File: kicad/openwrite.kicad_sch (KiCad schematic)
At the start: 77 parts, among them J1 raspberry-pi-zero-with-test-p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, SW71 SW_SPST, U1 adafruit-kb2040, U2 adafruit-powerboost-1000c, U3 waveshare-2in-lcd-st7789v

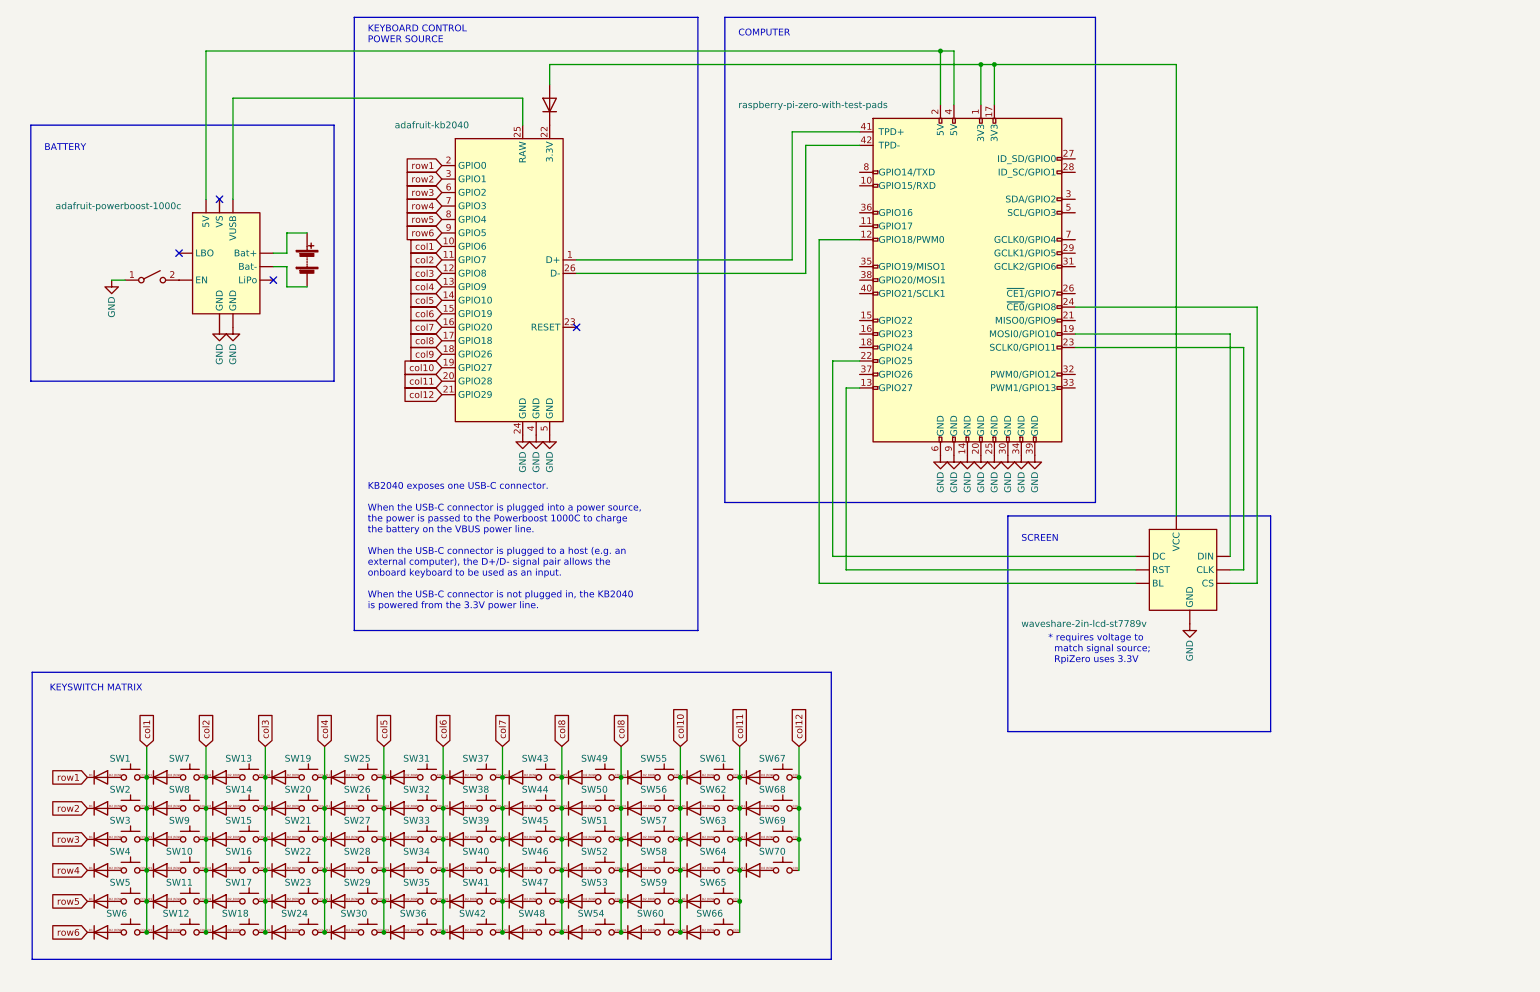
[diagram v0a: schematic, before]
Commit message: clean up schema, fix typos
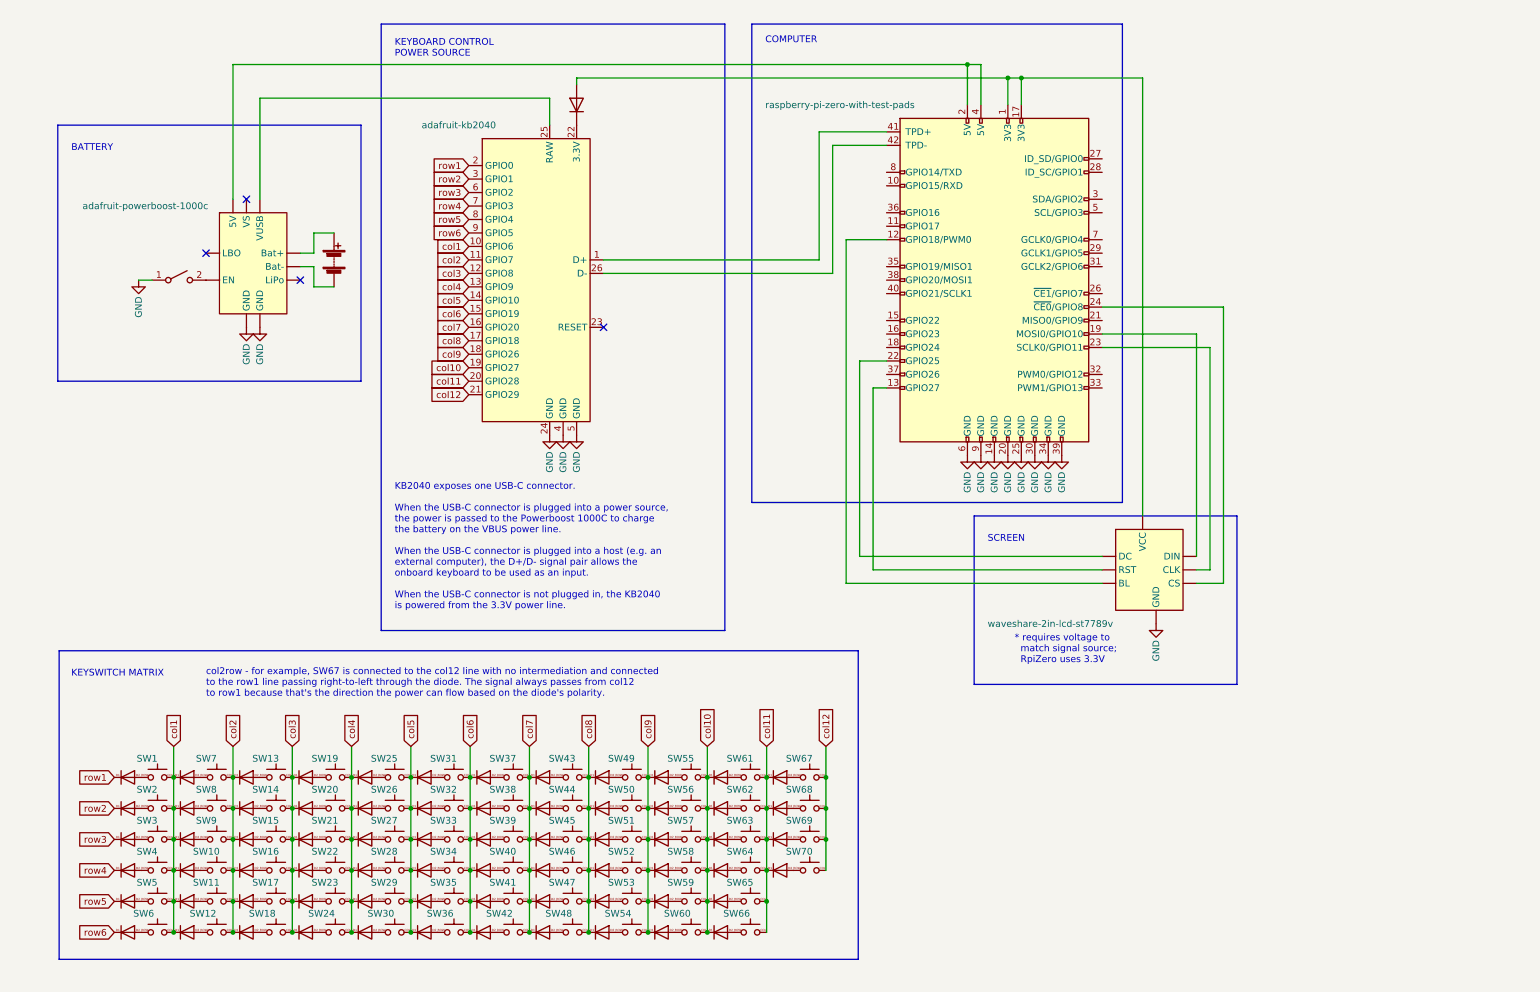
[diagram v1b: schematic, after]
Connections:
- net col8: no longer SW49.COL, SW50.COL, SW51.COL, SW52.COL, SW53.COL, SW54.COL, SW55.D1, SW56.D1, SW57.D1, SW58.D1, SW59.D1, SW60.D1
- net col9: now also SW49.COL, SW50.COL, SW51.COL, SW52.COL, SW53.COL, SW54.COL, SW55.D1, SW56.D1, SW57.D1, SW58.D1, SW59.D1, SW60.D1
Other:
- note added: "KB2040 exposes one USB-C connector. When the USB-C connector is plugged into a power source, the power is passed to the Powerboost 1000C to charge the battery on the VBUS power line. When the USB-C connector is plugged into a host (e.g. an external computer), the D+/D- signal pair allows the onboard keyboard to be used as an input. When the USB-C connector is not plugged in, the KB2040 is powered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"
- note added: "col2row - for example, SW67 is connected to the col12 line with no intermediation and connected to the row1 line passing right-to-left through the diode. The signal always passes from col12 to row1 because that's the direction the power can flow based on the diode's polarity."
- note removed: "KB2040 exposes one USB-C connector. When the USB-C connector is plugged into a power source, the power is passed to the Powerboost 1000C to charge the battery on the VBUS power line. When the USB-C connector is plugged to a host (e.g. an external computer), the D+/D- signal pair allows the onboard keyboard to be used as an input. When the USB-C connector is not plugged in, the KB2040 is powered f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"
- moved on the sheet: SW1, SW10, SW11, SW12, SW13, SW14, SW15, SW16, SW17, SW18, SW19, SW2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

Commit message: fix gateron-ks-33-diode symbol to remove extra pin
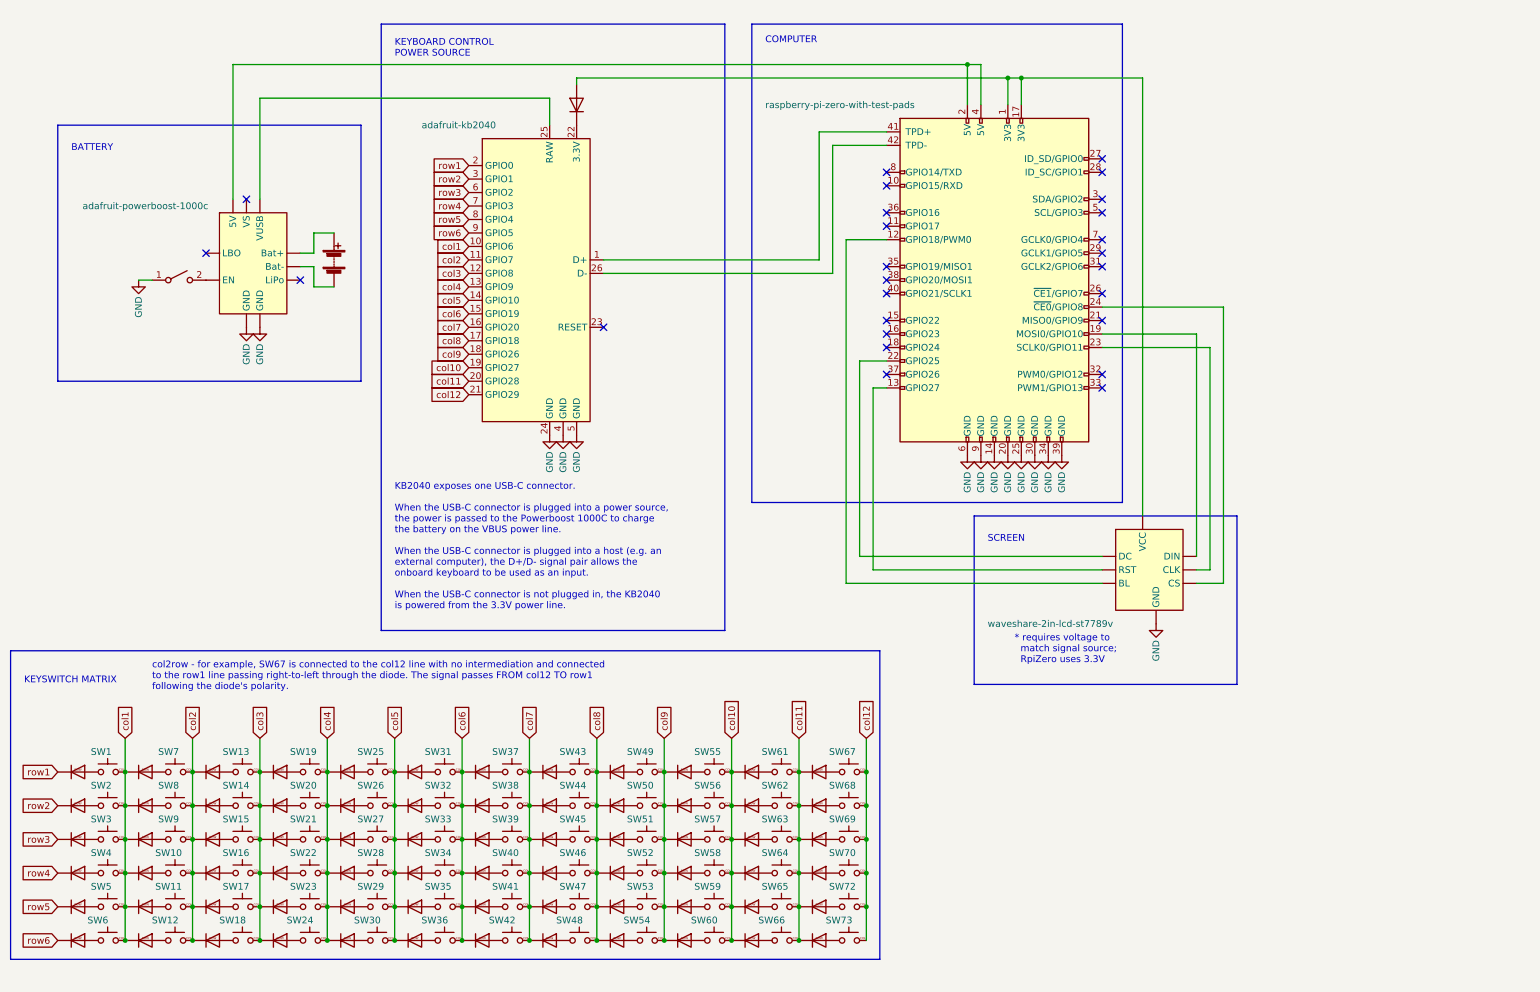
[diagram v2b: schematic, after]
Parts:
- added SW72, SW73: ~, openwrite:gateron-ks-33-diode, symbol openwrite:gateron-ks-33-diode
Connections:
- net col1: now also SW10.ROW, SW11.ROW, SW12.ROW, SW7.ROW, SW8.ROW, SW9.ROW; no longer SW10.D1, SW11.D1, SW12.D1, SW7.D1, SW8.D1, SW9.D1
- net col10: now also SW61.ROW, SW62.ROW, SW63.ROW, SW64.ROW, SW65.ROW, SW66.ROW; no longer SW61.D1, SW62.D1, SW63.D1, SW64.D1, SW65.D1, SW66.D1
- net col11: now also SW67.ROW, SW68.ROW, SW69.ROW, SW70.ROW, SW72.ROW, SW73.ROW; no longer SW67.D1, SW68.D1, SW69.D1, SW70.D1
- net col12: now also SW72.COL, SW73.COL
- net col2: now also SW13.ROW, SW14.ROW, SW15.ROW, SW16.ROW, SW17.ROW, SW18.ROW; no longer SW13.D1, SW14.D1, SW15.D1, SW16.D1, SW17.D1, SW18.D1
- net col3: now also SW19.ROW, SW20.ROW, SW21.ROW, SW22.ROW, SW23.ROW, SW24.ROW; no longer SW19.D1, SW20.D1, SW21.D1, SW22.D1, SW23.D1, SW24.D1
- net col4: now also SW25.ROW, SW26.ROW, SW27.ROW, SW28.ROW, SW29.ROW, SW30.ROW; no longer SW25.D1, SW26.D1, SW27.D1, SW28.D1, SW29.D1, SW30.D1
- net col5: now also SW31.ROW, SW32.ROW, SW33.ROW, SW34.ROW, SW35.ROW, SW36.ROW; no longer SW31.D1, SW32.D1, SW33.D1, SW34.D1, SW35.D1, SW36.D1
- net col6: now also SW37.ROW, SW38.ROW, SW39.ROW, SW40.ROW, SW41.ROW, SW42.ROW; no longer SW37.D1, SW38.D1, SW39.D1, SW40.D1, SW41.D1, SW42.D1
- net col7: now also SW43.ROW, SW44.ROW, SW45.ROW, SW46.ROW, SW47.ROW, SW48.ROW; no longer SW43.D1, SW44.D1, SW45.D1, SW46.D1, SW47.D1, SW48.D1
- net col8: now also SW49.ROW, SW50.ROW, SW51.ROW, SW52.ROW, SW53.ROW, SW54.ROW; no longer SW49.D1, SW50.D1, SW51.D1, SW52.D1, SW53.D1, SW54.D1
- net col9: now also SW55.ROW, SW56.ROW, SW57.ROW, SW58.ROW, SW59.ROW, SW60.ROW; no longer SW55.D1, SW56.D1, SW57.D1, SW58.D1, SW59.D1, SW60.D1
- net row1: now also SW1.ROW; no longer SW1.D1
- net row2: now also SW2.ROW; no longer SW2.D1
- net row3: now also SW3.ROW; no longer SW3.D1
- net row4: now also SW4.ROW; no longer SW4.D1
- net row5: now also SW5.ROW; no longer SW5.D1
- net row6: now also SW6.ROW; no longer SW6.D1
- no-connect marks 4 -> 26
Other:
- note added: "col2row - for example, SW67 is connected to the col12 line with no intermediation and connected to the row1 line passing right-to-left through the diode. The signal passes FROM col12 TO row1 following the diode's polarity."
- note removed: "col2row - for example, SW67 is connected to the col12 line with no intermediation and connected to the row1 line passing right-to-left through the diode. The signal always passes from col12 to row1 because that's the direction the power can flow based on the diode's polarity."

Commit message: Differentiate diode and keyswitch
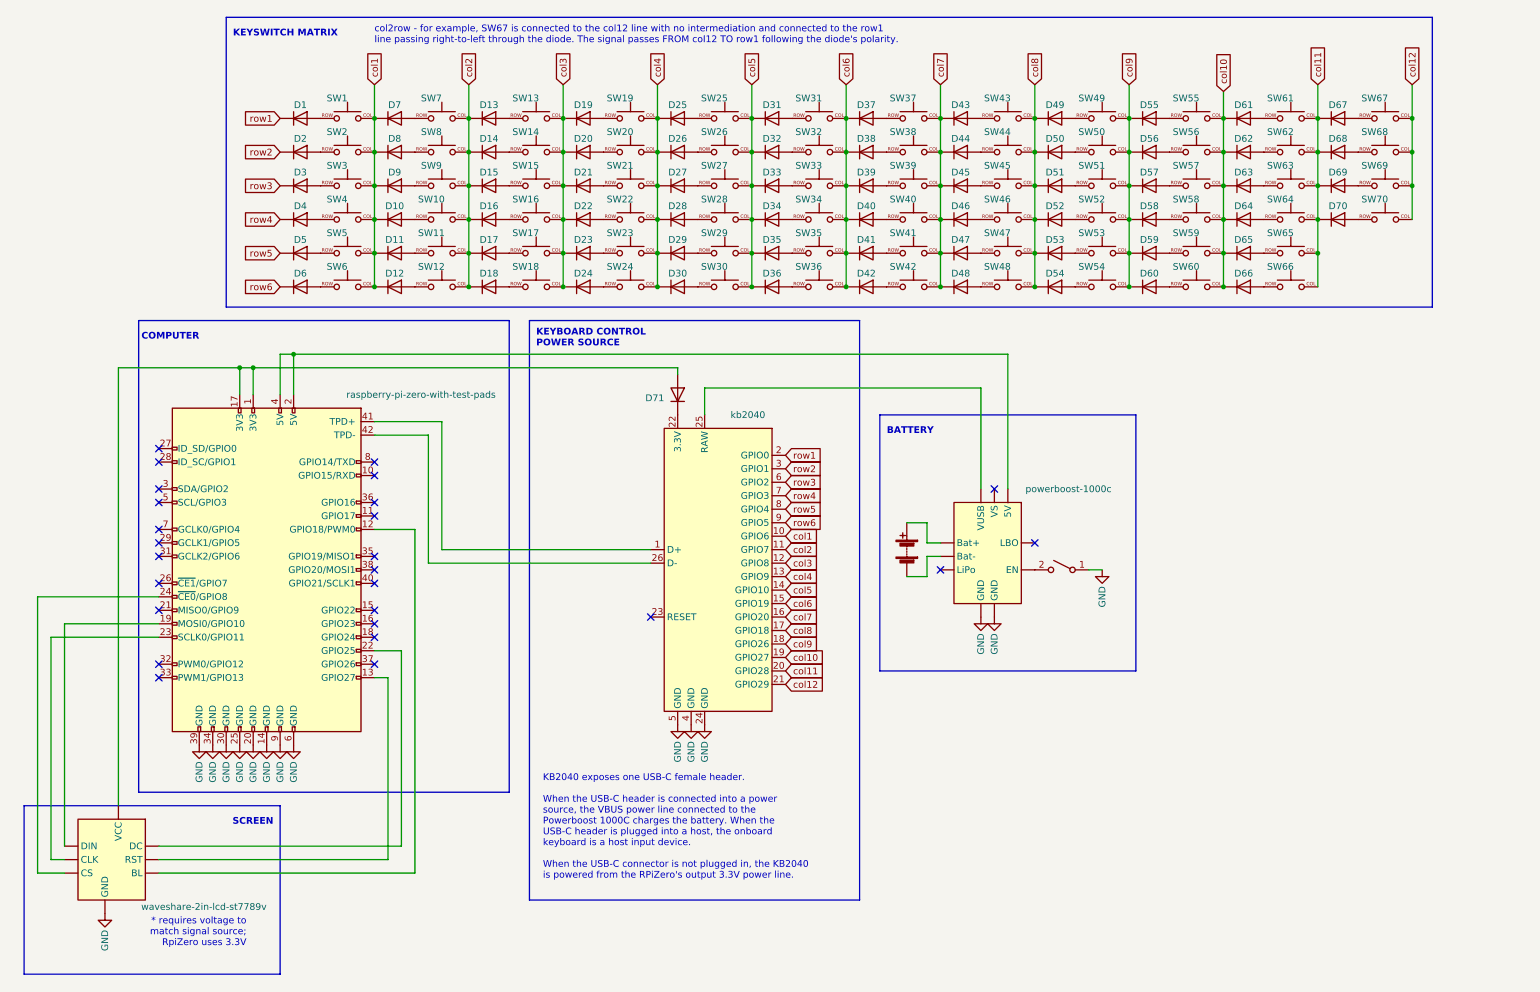
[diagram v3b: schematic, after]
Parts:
- removed D1: 1N4148, Diode_THT:D_DO-35_SOD27_P7.62mm_Horizontal, symbol Diode:1N4148
- removed SW10, SW11, SW12, SW13, SW14, SW15, SW16, SW17, SW18, SW19, SW2, SW20, SW21, SW22, SW23, SW24, SW25, SW26, SW27, SW28, SW29, SW3, SW30, SW31, SW32, SW33, SW34, SW35, SW36, SW37, SW38, SW39, SW4, SW40, SW41, SW42, SW43, SW44, SW45, SW46, SW47, SW48, SW49, SW5, SW50, SW51, SW52, SW53, SW54, SW55, SW56, SW57, SW58, SW59, SW6, SW60, SW61, SW62, SW63, SW64, SW65, SW66, SW67, SW68, SW69, SW7, SW70, SW72, SW73, SW8, SW9: ~, openwrite:gateron-ks-33-diode, symbol openwrite:gateron-ks-33-diode
- added D1, D10, D11, D12, D13, D14, D15, D16, D17, D18, D19, D2, D20, D21, D22, D23, D24, D25, D26, D27, D28, D29, D3, D30, D31, D32, D33, D34, D35, D36, D37, D38, D39, D4, D40, D41, D42, D43, D44, D45, D46, D47, D48, D49, D5, D50, D51, D52, D53, D54, D55, D56, D57, D58, D59, D6, D60, D61, D62, D63, D64, D65, D66, D67, D68, D69, D7, D70, D71, D8, D9: 1N4148, Diode_THT:D_DO-35_SOD27_P7.62mm_Horizontal, symbol openwrite:1N4148
- added SW10, SW11, SW12, SW13, SW14, SW15, SW16, SW17, SW18, SW19, SW2, SW20, SW21, SW22, SW23, SW24, SW25, SW26, SW27, SW28, SW29, SW3, SW30, SW31, SW32, SW33, SW34, SW35, SW36, SW37, SW38, SW39, SW4, SW40, SW41, SW42, SW43, SW44, SW45, SW46, SW47, SW48, SW49, SW5, SW50, SW51, SW52, SW53, SW54, SW55, SW56, SW57, SW58, SW59, SW6, SW60, SW61, SW62, SW63, SW64, SW65, SW66, SW67, SW68, SW69, SW7, SW70, SW8, SW9: ~, openwrite:gateron-ks-33, symbol openwrite:gateron-ks-33
- SW1: footprint openwrite:gateron-ks-33-diode -> openwrite:gateron-ks-33; symbol openwrite:gateron-ks-33-diode -> openwrite:gateron-ks-33
- U1: value adafruit-kb2040 -> kb2040
- U2: value adafruit-powerboost-1000c -> powerboost-1000c
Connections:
- net col1: now also D10.D1 (K), D11.D1 (K), D12.D1 (K), D7.D1 (K), D8.D1 (K), D9.D1 (K), SW2.COL, SW3.COL, SW4.COL, SW5.COL, SW6.COL
- net col10: now also D61.D1 (K), D62.D1 (K), D63.D1 (K), D64.D1 (K), D65.D1 (K), D66.D1 (K), SW55.COL, SW56.COL, SW57.COL, SW58.COL, SW59.COL, SW60.COL
- net col11: now also D67.D1 (K), D68.D1 (K), D69.D1 (K), D70.D1 (K), SW61.COL, SW62.COL, SW63.COL, SW64.COL, SW65.COL, SW66.COL
- net col12: now also SW67.COL, SW68.COL, SW69.COL, SW70.COL
- net col2: now also D13.D1 (K), D14.D1 (K), D15.D1 (K), D16.D1 (K), D17.D1 (K), D18.D1 (K), SW10.COL, SW11.COL, SW12.COL, SW7.COL, SW8.COL, SW9.COL
- net col3: now also D19.D1 (K), D20.D1 (K), D21.D1 (K), D22.D1 (K), D23.D1 (K), D24.D1 (K), SW13.COL, SW14.COL, SW15.COL, SW16.COL, SW17.COL, SW18.COL
- net col4: now also D25.D1 (K), D26.D1 (K), D27.D1 (K), D28.D1 (K), D29.D1 (K), D30.D1 (K), SW19.COL, SW20.COL, SW21.COL, SW22.COL, SW23.COL, SW24.COL
- net col5: now also D31.D1 (K), D32.D1 (K), D33.D1 (K), D34.D1 (K), D35.D1 (K), D36.D1 (K), SW25.COL, SW26.COL, SW27.COL, SW28.COL, SW29.COL, SW30.COL
- net col6: now also D37.D1 (K), D38.D1 (K), D39.D1 (K), D40.D1 (K), D41.D1 (K), D42.D1 (K), SW31.COL, SW32.COL, SW33.COL, SW34.COL, SW35.COL, SW36.COL
- net col7: now also D43.D1 (K), D44.D1 (K), D45.D1 (K), D46.D1 (K), D47.D1 (K), D48.D1 (K), SW37.COL, SW38.COL, SW39.COL, SW40.COL, SW41.COL, SW42.COL
- net col8: now also D49.D1 (K), D50.D1 (K), D51.D1 (K), D52.D1 (K), D53.D1 (K), D54.D1 (K), SW43.COL, SW44.COL, SW45.COL, SW46.COL, SW47.COL, SW48.COL
- net col9: now also D55.D1 (K), D56.D1 (K), D57.D1 (K), D58.D1 (K), D59.D1 (K), D60.D1 (K), SW49.COL, SW50.COL, SW51.COL, SW52.COL, SW53.COL, SW54.COL
- net row1: now also D1.D1 (K); no longer SW1.ROW
- net row2: now also D2.D1 (K)
- net row3: now also D3.D1 (K)
- net row4: now also D4.D1 (K)
- net row5: now also D5.D1 (K)
- net row6: now also D6.D1 (K)
- net at U1.22 (3.3V): now also D71.D1 (K)
- net at J1.1 (3V3), J1.17 (3V3), U3. (VCC): now also D71.D2 (A)
- new net: D29.D2 (A), SW29.ROW
- new net: D49.D2 (A), SW49.ROW
- new net: D70.D2 (A), SW70.ROW
- new net: D50.D2 (A), SW50.ROW
- new net: D15.D2 (A), SW15.ROW
- new net: D64.D2 (A), SW64.ROW
- new net: D47.D2 (A), SW47.ROW
- new net: D62.D2 (A), SW62.ROW
- new net: D40.D2 (A), SW40.ROW
- new net: D68.D2 (A), SW68.ROW
- new net: D2.D2 (A), SW2.ROW
- new net: D58.D2 (A), SW58.ROW
- new net: D26.D2 (A), SW26.ROW
- new net: D30.D2 (A), SW30.ROW
- new net: D51.D2 (A), SW51.ROW
- new net: D5.D2 (A), SW5.ROW
- new net: D16.D2 (A), SW16.ROW
- new net: D56.D2 (A), SW56.ROW
- new net: D35.D2 (A), SW35.ROW
- new net: D65.D2 (A), SW65.ROW
- new net: D23.D2 (A), SW23.ROW
- new net: D14.D2 (A), SW14.ROW
- new net: D55.D2 (A), SW55.ROW
- new net: D69.D2 (A), SW69.ROW
- new net: D63.D2 (A), SW63.ROW
- new net: D54.D2 (A), SW54.ROW
- new net: D53.D2 (A), SW53.ROW
- new net: D67.D2 (A), SW67.ROW
- new net: D48.D2 (A), SW48.ROW
- new net: D22.D2 (A), SW22.ROW
- new net: D11.D2 (A), SW11.ROW
- new net: D60.D2 (A), SW60.ROW
- new net: D34.D2 (A), SW34.ROW
- new net: D24.D2 (A), SW24.ROW
- new net: D61.D2 (A), SW61.ROW
- new net: D37.D2 (A), SW37.ROW
- new net: D31.D2 (A), SW31.ROW
- new net: D38.D2 (A), SW38.ROW
- new net: D8.D2 (A), SW8.ROW
- new net: D3.D2 (A), SW3.ROW
- new net: D21.D2 (A), SW21.ROW
- new net: D46.D2 (A), SW46.ROW
- new net: D9.D2 (A), SW9.ROW
- new net: D52.D2 (A), SW52.ROW
- new net: D20.D2 (A), SW20.ROW
- new net: D18.D2 (A), SW18.ROW
- new net: D32.D2 (A), SW32.ROW
- new net: D66.D2 (A), SW66.ROW
- new net: D28.D2 (A), SW28.ROW
- new net: D10.D2 (A), SW10.ROW
- new net: D25.D2 (A), SW25.ROW
- new net: D27.D2 (A), SW27.ROW
- new net: D17.D2 (A), SW17.ROW
- new net: D4.D2 (A), SW4.ROW
- new net: D45.D2 (A), SW45.ROW
- new net: D33.D2 (A), SW33.ROW
- new net: D44.D2 (A), SW44.ROW
- new net: D19.D2 (A), SW19.ROW
- new net: D1.D2 (A), SW1.ROW
- new net: D57.D2 (A), SW57.ROW
- new net: D42.D2 (A), SW42.ROW
- new net: D12.D2 (A), SW12.ROW
- new net: D41.D2 (A), SW41.ROW
- new net: D59.D2 (A), SW59.ROW
- new net: D43.D2 (A), SW43.ROW
- new net: D36.D2 (A), SW36.ROW
- new net: D6.D2 (A), SW6.ROW
- new net: D39.D2 (A), SW39.ROW
- new net: D7.D2 (A), SW7.ROW
- new net: D13.D2 (A), SW13.ROW
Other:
- note added: "KB2040 exposes one USB-C female header. When the USB-C header is connected into a power source, the VBUS power line connected to the Powerboost 1000C charges the battery. When the USB-C header is plugged into a host, the onboard keyboard is a host input device. When the USB-C connector is not plugged in, the KB2040 is powered from the RPiZero's output 3.3V power line."
- note removed: "KB2040 exposes one USB-C connector. When the USB-C connector is plugged into a power source, the power is passed to the Powerboost 1000C to charge the battery on the VBUS power line. When the USB-C connector is plugged into a host (e.g. an external computer), the D+/D- signal pair allows the onboard keyboard to be used as an input. When the USB-C connector is not plugged in, the KB2040 is powered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"
